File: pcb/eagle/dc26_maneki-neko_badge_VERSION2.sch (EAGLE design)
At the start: 53 parts, among them SW1 PTS645SM43SMTR92, T1 RK7002BMT116, U1 STM32F030C8T, U2 PAM2301CAAB330, U3 NPTC042KFMS-RC

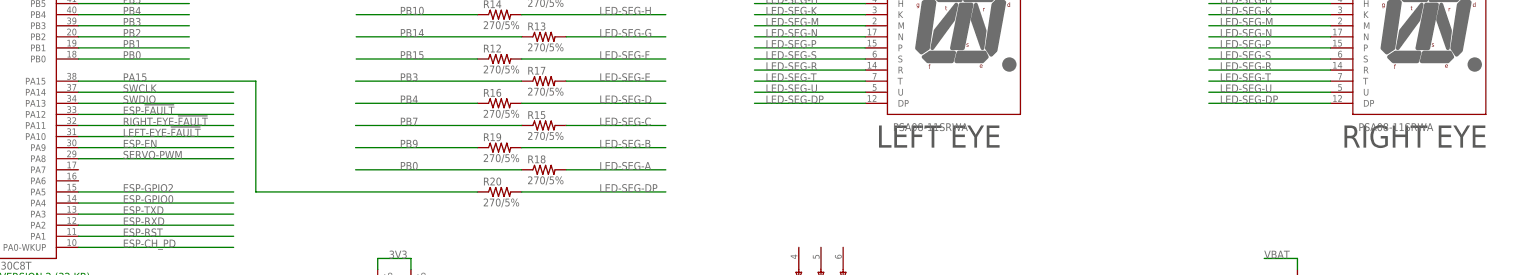
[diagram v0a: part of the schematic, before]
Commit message: pcb v2 routed, bom edited, gerbers rendered - quote out to pcba house and dfm check to freedfm
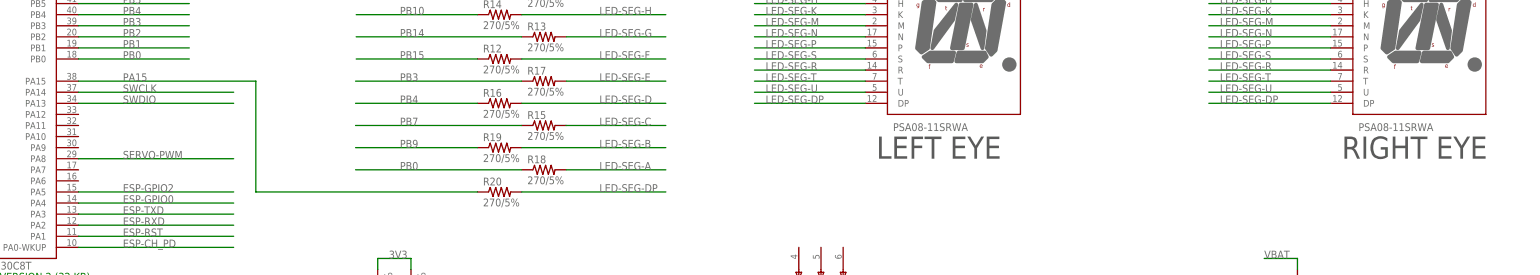
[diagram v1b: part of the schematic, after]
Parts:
- renumbered U$2 to H4
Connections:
- removed net ESP-!FAULT: U1MCU.PA12
- removed net ESP-EN: U1MCU.PA9
- removed net LEFT-EYE-!FAULT: U1MCU.PA10
- removed net RIGHT-EYE-!FAULT: U1MCU.PA11
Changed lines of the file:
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@@
 <part name="SW1" library="PTS645SM43SMTR92" deviceset="PTS645SM43SMTR92" device=""/>
 <part name="S1" library="JS202011SCQN" deviceset="JS202011SCQN" device=""/>
-<part name="U$2" library="battery_pads" deviceset="BATTPADS-SMT" device=""/>
+<part name="H4" library="battery_pads" deviceset="BATTPADS-SMT" device=""/>
 <part name="S2" library="JS202011SCQN" deviceset="JS202011SCQN" device=""/>
 <part name="R30" library="rcl" library_urn="urn:adsk.eagle:library:334" deviceset="R-US_" device="R0805" package3d_urn="urn:adsk.eagle:package:23553/2" value="10k/5%"/>
@@
 <sheet>
 <plain>
-<text x="167.64" y="119.38" size="5.08" layer="97">RIGHT EYE</text>
-<text x="60.96" y="119.38" size="5.08" layer="97">LEFT EYE</text>
+<text x="167.64" y="116.84" size="5.08" layer="97">RIGHT EYE</text>
+<text x="60.96" y="116.84" size="5.08" layer="97">LEFT EYE</text>
 <text x="-35.56" y="195.58" size="1.778" layer="97">(3.3V - 2V) / 270 ohms = 5 mA</text>
 <text x="154.94" y="43.18" size="5.08" layer="97">SERVO DRIVE</text>
@@
 <instance part="SW1" gate="G$1" x="-210.82" y="127"/>
 <instance part="S1" gate="G$1" x="-177.8" y="241.3"/>
-<instance part="U$2" gate="G$1" x="-208.28" y="226.06" rot="MR0"/>
+<instance part="H4" gate="G$1" x="-208.28" y="226.06" rot="MR0"/>
 <instance part="S2" gate="G$1" x="48.26" y="83.82" smashed="yes">
 <attribute name="NAME" x="58.3908" y="81.28486875" size="1.272440625" layer="95"/>
@@
 <segment>
 <pinref part="SUPPLY1" gate="GND" pin="GND"/>
-<pinref part="U$2" gate="G$1" pin="2"/>
+<pinref part="H4" gate="G$1" pin="2"/>
 <wire x1="-203.2" y1="223.52" x2="-165.1" y2="223.52" width="0.1524" layer="91"/>
 </segment>
@@
 </segment>
 </net>
-<net name="LEFT-EYE-!FAULT" class="0">
-<segment>
-<pinref part="U1" gate="MCU" pin="PA10"/>
-<wire x1="-121.92" y1="121.92" x2="-86.36" y2="121.92" width="0.1524" layer="91"/>
-<label x="-111.76" y="121.92" size="1.778" layer="95"/>
-</segment>
-</net>
 <net name="!RESET" class="0">
 <segment>
@@
 <label x="-119.38" y="63.5" size="1.778" layer="95" rot="MR0"/>
 <pinref part="H1" gate="G$1" pin="9"/>
-</segment>
-</net>
-<net name="ESP-EN" class="0">
-<segment>
-<pinref part="U1" gate="MCU" pin="PA9"/>
-<wire x1="-86.36" y1="119.38" x2="-121.92" y2="119.38" width="0.1524" layer="91"/>
-<label x="-111.76" y="119.38" size="1.778" layer="95"/>
-</segment>
-</net>
-<net name="ESP-!FAULT" class="0">
-<segment>
-<pinref part="U1" gate="MCU" pin="PA12"/>
-<wire x1="-121.92" y1="127" x2="-86.36" y2="127" width="0.1524" layer="91"/>
-<label x="-111.76" y="127" size="1.778" layer="95"/>
-</segment>
-</net>
-<net name="RIGHT-EYE-!FAULT" class="0">
-<segment>
-<pinref part="U1" gate="MCU" pin="PA11"/>
-<wire x1="-86.36" y1="124.46" x2="-121.92" y2="124.46" width="0.1524" layer="91"/>
-<label x="-111.76" y="124.46" size="1.778" layer="95"/>
 </segment>
 </net>
@@
 <net name="VBATIN" class="0">
 <segment>
-<pinref part="U$2" gate="G$1" pin="1"/>
+<pinref part="H4" gate="G$1" pin="1"/>
 <wire x1="-203.2" y1="226.06" x2="-177.8" y2="226.06" width="0.1524" layer="91"/>
 <pinref part="S1" gate="G$1" pin="2"/>
